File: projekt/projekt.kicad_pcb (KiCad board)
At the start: 2 copper layers, 28 parts, among them J1 Conn_01x05, J2 Conn_01x04, J4 87583-0010RHLF, J5 10118192-0001LF, U1 MAX17048G_T10, U2 TPS61022RWUT, U3 MCP73871-2CCI_ML

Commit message: MAIN: wersja pierwsza 19.04.
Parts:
- added R11: R, Resistor_SMD:R_0603_1608Metric, F.Cu at (166.2, 72.9)
- added R12: R, Resistor_SMD:R_0603_1608Metric, F.Cu at (169.8, 77.0)
- added R13: R, Resistor_SMD:R_0603_1608Metric, F.Cu at (169.8, 72.9)
- added R8: R, Resistor_SMD:R_0603_1608Metric, F.Cu at (166.2, 77.0)
- added REF**: MountingHole_2mm, MountingHole:MountingHole_2mm, F.Cu at (180.4, 45.6)
- added REF**: MountingHole_2mm, MountingHole:MountingHole_2mm, F.Cu at (95.4, 85.6)
- added REF**: MountingHole_2mm, MountingHole:MountingHole_2mm, F.Cu at (95.4, 45.6)
- added REF**: MountingHole_2mm, MountingHole:MountingHole_2mm, F.Cu at (180.4, 85.6)
- moved J5 96.6 mm to (87.9, 74.9), turned to -90 degrees
- moved J4 74.8 mm to (178.6, 73.8), turned to 90 degrees
- moved C8 46.4 mm to (127.1, 72.5), turned to 180 degrees
- moved C4 42.8 mm to (160.7, 73.1), turned to -90 degrees
- moved C5 41.9 mm to (127.1, 75.0), turned to 180 degrees
- moved R9 40.4 mm to (132.9, 68.7), turned to 90 degrees
- moved R10 38.0 mm to (135.4, 68.7), turned to 90 degrees
- moved R6 38.0 mm to (126.9, 81.0), turned to -90 degrees
- moved C9 37.4 mm to (127.1, 77.5)
- moved R2 36.7 mm to (111.2, 79.9)
- moved R1 36.3 mm to (111.2, 77.3)
- moved U3 34.9 mm to (133.3, 74.7), turned to 90 degrees
- moved R5 34.6 mm to (129.9, 81.0), turned to 90 degrees
- moved U2 34.1 mm to (156.3, 73.2), turned to 180 degrees
- moved R4 34.0 mm to (155.9, 69.2), turned to 180 degrees
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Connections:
- J4 pad 02: unconnected-(J4-D--Pad02) -> /D-
- J4 pad 03: unconnected-(J4-D+-Pad03) -> /D+
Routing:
- net +5V_CHARGE: track 0.00 -> 81.7 mm, vias 0 -> 2
- net GND: track 8.02 -> 57.8 mm, vias 0 -> 28
- net +BATT: track 2.54 -> 47.4 mm
- net V_LOAD: track 0.00 -> 35.4 mm, vias 0 -> 2
- net +5V_OUT: track 0.00 -> 17.5 mm
- net /D+: track 0.00 -> 11.8 mm
- net /INT: track 5.35 -> 13.8 mm
- net Net-(U3-VPCC): track 0.00 -> 8.42 mm
- net /D-: track 0.00 -> 8.41 mm
- net Net-(RT1-Pad2): track 0.00 -> 6.78 mm
- net V_IN_FG: track 28.6 -> 35.1 mm
- net /SCL: track 7.68 -> 13.8 mm
- net /SDA: track 8.94 -> 14.2 mm
- net Net-(U3-PROG3): track 0.00 -> 3.92 mm
- net Net-(U3-THERM): track 0.00 -> 3.87 mm
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- added copper zone on F.Cu, net +5V_CHARGE
- added copper zone on F.Cu, net +5V_OUT
- added copper zone on B.Cu, net GND
- added copper zone on F.Cu, net GND
- added copper zone on F.Cu, net Net-(U2-FB)
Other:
- board outline added: 100 x 45 mm
- board text added: "5V"
- board text added: "GND"
- board text added: "INT"
- board text added: "LBO"
- board text added: "PG"
- board text added: "SCL"
- board text added: "SDA"
- board text added: "STAT2"

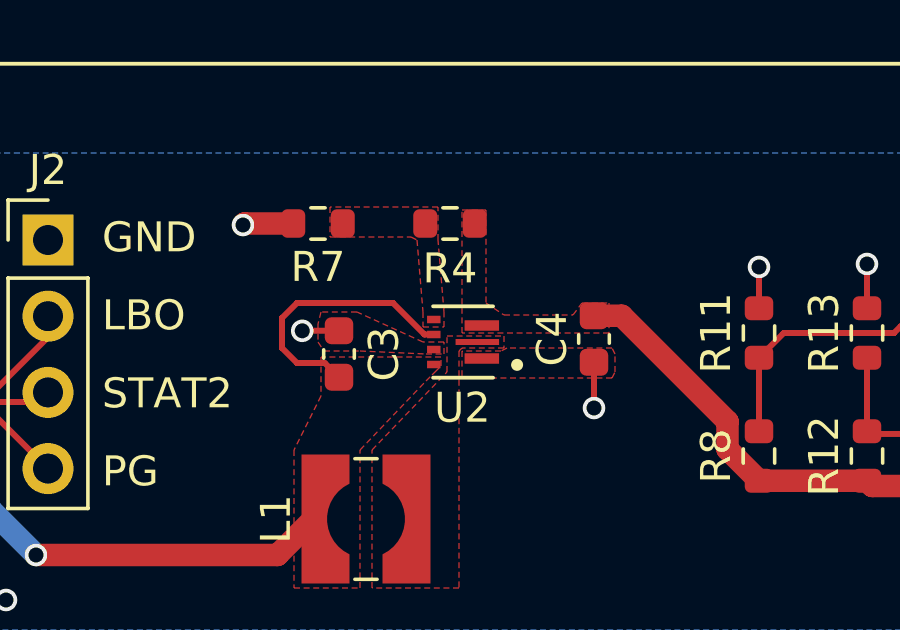
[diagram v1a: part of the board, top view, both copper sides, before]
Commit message: MAIN: 23.04 start wersja 2 - poprawki w schemacie.
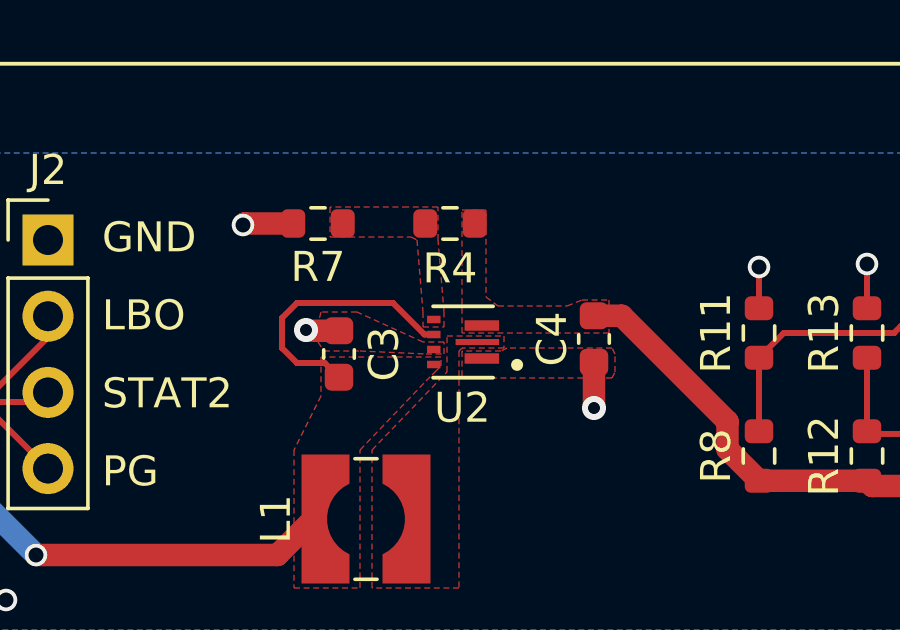
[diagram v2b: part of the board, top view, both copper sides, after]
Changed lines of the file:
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@@
   (segment (start 127.875 72.5) (end 127.875 72.562606) (width 0.75) (layer "F.Cu") (net 1))
   (segment (start 105.123402 53.6) (end 112.15 60.626598) (width 0.75) (layer "F.Cu") (net 1))
-  (segment (start 160.7 73.875) (end 160.7 75.4) (width 0.2) (layer "F.Cu") (net 2))
   (segment (start 149.05 69.25) (end 149 69.3) (width 0.75) (layer "F.Cu") (net 2))
   (segment (start 139.6 81.825) (end 141.075 81.825) (width 0.2) (layer "F.Cu") (net 2))
@@
   (segment (start 125.575 80.175) (end 125.5 80.1) (width 0.2) (layer "F.Cu") (net 2))
   (segment (start 126.9 80.175) (end 125.575 80.175) (width 0.2) (layer "F.Cu") (net 2))
-  (segment (start 152.2 72.825) (end 150.977298 72.825) (width 0.2) (layer "F.Cu") (net 2))
   (segment (start 135.5 72.5) (end 133.9 74.1) (width 0.75) (layer "F.Cu") (net 2))
-  (segment (start 150.977298 72.825) (end 150.975 72.827298) (width 0.2) (layer "F.Cu") (net 2))
   (segment (start 133.9 74.1) (end 133.9 74.2) (width 0.75) (layer "F.Cu") (net 2))
   (segment (start 117.945 74.255) (end 118.2 74) (width 0.2) (layer "F.Cu") (net 2))
   (segment (start 126.325 75) (end 124 75) (width 0.75) (layer "F.Cu") (net 2))
   (segment (start 177.07 57.77) (end 177.8 58.5) (width 0.75) (layer "F.Cu") (net 2))
+  (segment (start 160.7 73.875) (end 160.7 75.4) (width 0.75) (layer "F.Cu") (net 2))
   (segment (start 112.6 71.3) (end 111.5 72.4) (width 0.2) (layer "F.Cu") (net 2))
   (segment (start 85.2055 80.2055) (end 85.9 80.9) (width 0.75) (layer "F.Cu") (net 2))
@@
   (segment (start 150.675 69.25) (end 149.05 69.25) (width 0.75) (layer "F.Cu") (net 2))
   (segment (start 141.075 81.825) (end 141.1 81.8) (width 0.2) (layer "F.Cu") (net 2))
+  (segment (start 151.125 72.825) (end 151.1 72.8) (width 0.75) (layer "F.Cu") (net 2))
   (segment (start 133.8 74.2) (end 133.3 74.7) (width 0.75) (layer "F.Cu") (net 2))
   (segment (start 85.9055 71.78075) (end 85.2055 71.08075) (width 0.75) (layer "F.Cu") (net 2))
@@
   (segment (start 112.625 71.3) (end 112.6 71.3) (width 0.2) (layer "F.Cu") (net 2))
   (segment (start 85.2055 78.68075) (end 85.2055 80.2055) (width 0.75) (layer "F.Cu") (net 2))
+  (segment (start 152.2 72.825) (end 151.125 72.825) (width 0.75) (layer "F.Cu") (net 2))
   (segment (start 85.2055 78.68075) (end 85.2055 76.08075) (width 0.75) (layer "F.Cu") (net 2))
   (segment (start 126.325 77.675) (end 125.4 78.6) (width 0.75) (layer "F.Cu") (net 2))
@@
   (segment (start 116.375 75.24) (end 118.16 75.24) (width 0.75) (layer "F.Cu") (net 2))
   (segment (start 89.40575 76.30575) (end 87.8805 76.30575) (width 0.75) (layer "F.Cu") (net 2))
+  (via (at 151.1 72.8) (size 0.8) (drill 0.4) (layers "F.Cu" "B.Cu") (net 2))
   (via (at 111.5 72.4) (size 0.75) (drill 0.5) (layers "F.Cu" "B.Cu") (net 2))
+  (via (at 160.7 75.4) (size 0.8) (drill 0.4) (layers "F.Cu" "B.Cu") (net 2))
   (via (at 131.6 67.5) (size 0.75) (drill 0.5) (layers "F.Cu" "B.Cu") (net 2))
   (via (at 141.1 81.8) (size 0.75) (drill 0.5) (layers "F.Cu" "B.Cu") (net 2))
@@
   (via (at 90.1 77) (size 0.75) (drill 0.5) (layers "F.Cu" "B.Cu") (free) (net 2))
   (via (at 125.5 80.1) (size 0.75) (drill 0.5) (layers "F.Cu" "B.Cu") (net 2))
-  (via (at 160.7 75.4) (size 0.75) (drill 0.5) (layers "F.Cu" "B.Cu") (net 2))
   (via (at 133.9 75.3) (size 0.75) (drill 0.5) (layers "F.Cu" "B.Cu") (net 2))
   (via (at 118.2 75.2) (size 0.75) (drill 0.5) (layers "F.Cu" "B.Cu") (net 2))
@@
   (via (at 123.9 75.1) (size 0.75) (drill 0.5) (layers "F.Cu" "B.Cu") (net 2))
   (via (at 135.5 72.5) (size 0.75) (drill 0.5) (layers "F.Cu" "B.Cu") (free) (net 2))
-  (via (at 150.975 72.827298) (size 0.75) (drill 0.5) (layers "F.Cu" "B.Cu") (net 2))
   (segment (start 104.335 80.673846) (end 104.335 73.8275) (width 0.2) (layer "F.Cu") (net 3))
   (segment (start 105.535 72.6275) (end 106.83 72.6275) (width 0.2) (layer "F.Cu") (net 3))
@@
         (xy 156.3 68.8)
         (xy 157.1 68.8)
-        (xy 157.1 71.9)
-        (xy 157.7 72.3)
-        (xy 160 72.3)
-        (xy 160.3 71.9)
-        (xy 161.2 71.9)
+        (xy 157.1 71.7)
+        (xy 157.5 72)
+        (xy 159.8 72)
+        (xy 160.3 71.8)
+        (xy 161.2 71.8)
         (xy 161.2 72.9)
       )

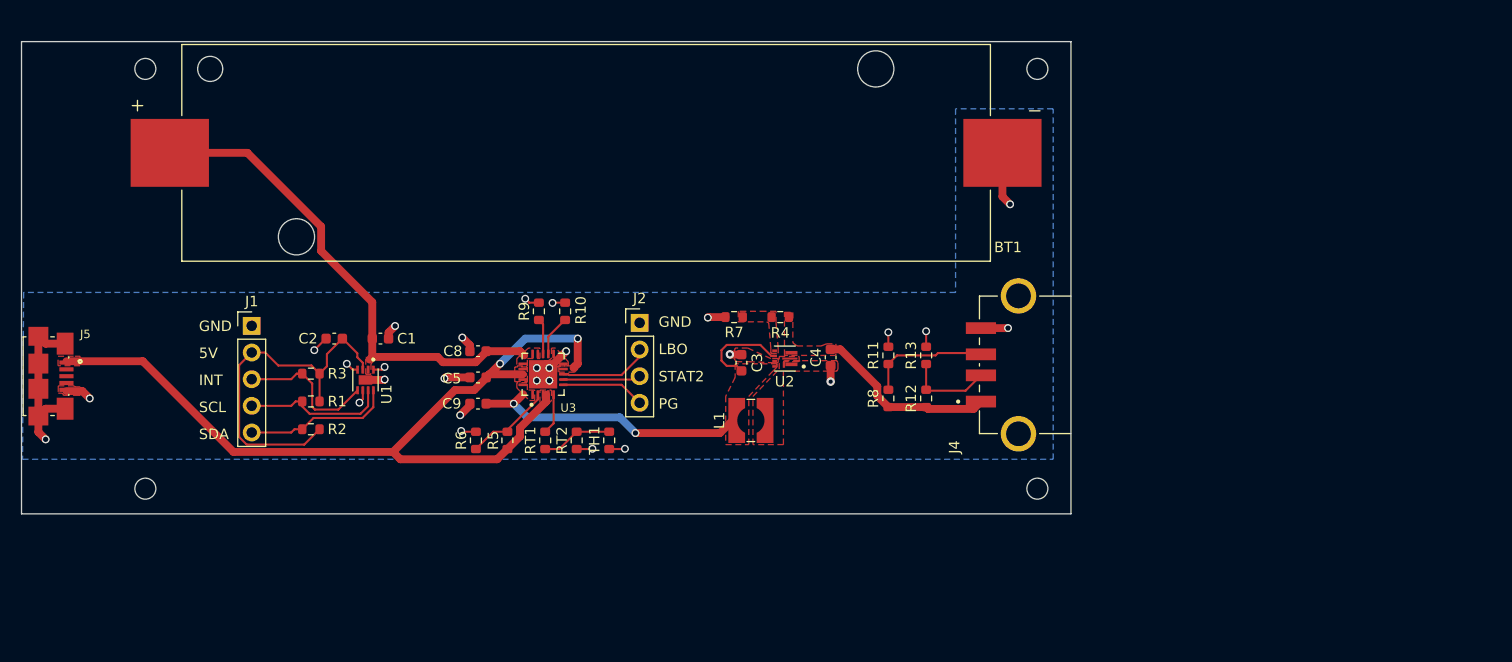
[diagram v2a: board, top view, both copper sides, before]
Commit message: MAIN: Wersja 2: poprawki sieci +5V_CHARGE.
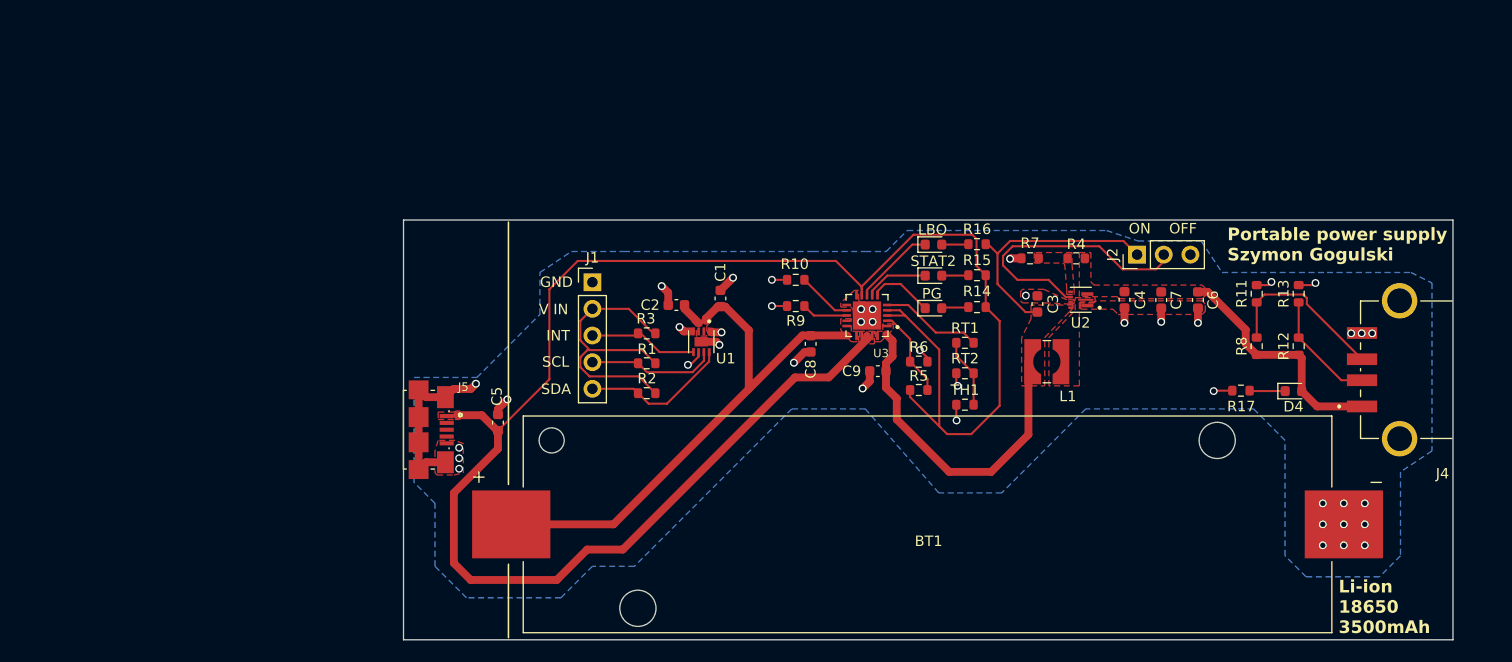
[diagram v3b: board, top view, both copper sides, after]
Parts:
- removed REF** (x4): MountingHole_2mm, MountingHole:MountingHole_2mm
- added C6: 22u, Capacitor_SMD:C_0603_1608Metric, F.Cu at (195.7, 67.6)
- added C7: 22u, Capacitor_SMD:C_0603_1608Metric, F.Cu at (192.2, 67.6)
- added D1: LED G, Diode_SMD:D_0603_1608Metric, F.Cu at (170.5, 68.4)
- added D2: LED Y, Diode_SMD:D_0603_1608Metric, F.Cu at (170.5, 65.3)
- added D3: LED Y, Diode_SMD:D_0603_1608Metric, F.Cu at (170.5, 62.3)
- added D4: LED B, Diode_SMD:D_0603_1608Metric, F.Cu at (204.8, 76.3)
- added R14: 470, Resistor_SMD:R_0603_1608Metric, F.Cu at (174.7, 68.3)
- added R15: 470, Resistor_SMD:R_0603_1608Metric, F.Cu at (174.7, 65.3)
- added R16: 470, Resistor_SMD:R_0603_1608Metric, F.Cu at (174.7, 62.3)
- added R17: 470, Resistor_SMD:R_0603_1608Metric, F.Cu at (199.8, 76.3)
- J2: value Conn_01x04 -> Conn_01x03; footprint Connector_PinHeader_2.54mm:PinHeader_1x04_P2.54mm_Vertical -> Connector_PinHeader_2.54mm:PinHeader_1x03_P2.54mm_Vertical
- R10: value 100k -> 20k
- R5: value 612k -> 330k
- R6: value 200k -> 110k
- R9: value 1k -> 570
- moved BT1 48.1 mm to (169.9, 89.0)
- moved J2 47.8 mm to (189.9, 63.3), turned to 90 degrees
- moved R6 42.9 mm to (169.1, 73.5), turned to 180 degrees
- moved RT1 41.1 mm to (173.5, 71.7), turned to 180 degrees
- moved R5 39.5 mm to (169.1, 76.2), turned to 0 degrees
- moved C9 38.2 mm to (165.2, 74.4)
- moved RT2 37.5 mm to (173.5, 74.6), turned to 180 degrees
- moved J5 36.6 mm to (124.1, 80.0)
- moved J4 36.3 mm to (214.9, 74.3)
- moved R13 36.0 mm to (205.3, 67.0)
- moved R12 35.8 mm to (205.3, 72.0)
- moved R11 35.6 mm to (201.3, 67.0)
- moved R8 35.5 mm to (201.3, 72.0)
- moved TH1 34.1 mm to (173.5, 77.6), turned to 0 degrees
- moved C2 32.8 mm to (146.0, 68.1)
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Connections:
- C2 pad 1: V_IN_FG -> +BATT
- J1 pad 2: V_IN_FG -> V_MCU_LOGIC
- J2 pad 1: GND -> V_LOAD
- J2 pad 2: /LBO -> /EN
- J2 pad 3: /STAT2 -> GND
- R1 pad 1: V_IN_FG -> V_MCU_LOGIC
- R2 pad 1: V_IN_FG -> V_MCU_LOGIC
- R3 pad 1: V_IN_FG -> V_MCU_LOGIC
- U1 pad 3: V_IN_FG -> +BATT
- U2 pad 5: V_LOAD -> /EN
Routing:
- net +5V_CHARGE: track 81.7 -> 174.4 mm, vias 2 -> 0
- net V_IN_FG: track 35.1 -> 0.00 mm
- net V_MCU_LOGIC: track 0.00 -> 28.9 mm
- net /EN: track 0.00 -> 26.2 mm
- net V_LOAD: track 35.4 -> 55.7 mm, vias 2 -> 0
- net GND: track 57.7 -> 49.5 mm, vias 28 -> 42
- net Net-(U3-THERM): track 3.87 -> 9.72 mm
- net +BATT: track 47.4 -> 53.1 mm
- net +5V_OUT: track 17.5 -> 22.8 mm
- net /D+: track 11.8 -> 16.6 mm
- net Net-(D4-K): track 0.00 -> 3.40 mm
- net /INT: track 13.8 -> 10.5 mm
- net /D-: track 8.41 -> 11.1 mm
- net Net-(D2-A): track 0.00 -> 2.65 mm
- net Net-(D1-A): track 0.00 -> 2.65 mm
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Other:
- board size 100 x 45 mm -> 100 x 40 mm
- board text added: "Li-ion 18650 3500mAh"
- board text added: "ON OFF"
- board text added: "Portable power supply Szymon Gogulski"
- board text added: "V IN"
- board text removed: "5V"

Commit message: MAIN: Wersja 2. Sprawdzenie reguł produkcyjnych. Test wykonania u producenta.
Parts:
- added H1: MountingHole, MountingHole:MountingHole_2.2mm_M2, F.Cu at (133.0, 63.0)
- added H2: MountingHole, MountingHole:MountingHole_2.2mm_M2, F.Cu at (217.0, 63.0)
- added H3: MountingHole, MountingHole:MountingHole_2.2mm_M2, F.Cu at (217.0, 97.0)
- added TP1: TestPoint, TestPoint:TestPoint_THTPad_1.0x1.0mm_Drill0.5mm, F.Cu at (147.1, 76.7)
- added TP2: TestPoint, TestPoint:TestPoint_THTPad_1.0x1.0mm_Drill0.5mm, F.Cu at (128.6, 74.0)
- added TP3: TestPoint, TestPoint:TestPoint_THTPad_1.0x1.0mm_Drill0.5mm, F.Cu at (189.6, 76.3)
- added TP4: TestPoint, TestPoint:TestPoint_THTPad_1.0x1.0mm_Drill0.5mm, F.Cu at (193.9, 73.6)
- added TP5: TestPoint, TestPoint:TestPoint_THTPad_D1.0mm_Drill0.5mm, F.Cu at (150.2, 76.7)
- added TP6: TestPoint, TestPoint:TestPoint_THTPad_D1.0mm_Drill0.5mm, F.Cu at (131.7, 74.0)
- added TP7: TestPoint, TestPoint:TestPoint_THTPad_D1.0mm_Drill0.5mm, F.Cu at (186.5, 76.3)
- added TP8: TestPoint, TestPoint:TestPoint_THTPad_D1.0mm_Drill0.5mm, F.Cu at (197.0, 73.6)
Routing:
- net V_LOAD: track 55.7 -> 63.8 mm
- net +5V_OUT: track 22.8 -> 26.8 mm
- net +5V_CHARGE: track 174.4 -> 178.0 mm
- net +BATT: track 53.1 -> 55.5 mm
- net V_MCU_LOGIC: track 28.9 -> 30.4 mm
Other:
- board text added: "BATT TP"
- board text added: "CHARGE TP"
- board text added: "LOAD TP"
- board text added: "OUT TP"

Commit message: MAIN: wersja 2, dodałem modele 3D.
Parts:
- L1: footprint Inductor_SMD:L_Wuerth_WE-TPC-3816 -> WE-TCP_3816:WE-TPC_3816
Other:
- board text added: "T° Sens"

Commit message: MAIN: wersja 2: Poprawiłem termistor, readme update.
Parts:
- moved TH1 9.60 mm to (173.5, 87.2)
- turned R5 to 180 degrees
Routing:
- net V_LOAD: track 63.8 -> 77.8 mm
- net +5V_CHARGE: track 178.0 -> 164.7 mm
- net Net-(RT1-Pad2): track 6.58 -> 16.2 mm
- net Net-(U3-VPCC): track 8.44 -> 7.76 mm
- net Net-(U3-THERM): track 9.72 -> 10.3 mm
